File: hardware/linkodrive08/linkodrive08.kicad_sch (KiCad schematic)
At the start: 101 parts, among them J1 USB_C_Receptacle_USB2.0_16P, J2 HALL, J3 WCH_SWD, J4 LKS_SWD, J5 MOT_POWER, J6 GATE_DRIVE, J7 LOGIC_POWER, J8 MOT, Q1 WSD4070DN, Q2 WSD4070DN, Q3 WSD4070DN, Q4 WSD4070DN, Q5 WSD4070DN, Q6 WSD4070DN, U1 LKS32MC086NxQx, U3 XL1509-ADJ, U4 TPS54260, Y1 Crystal_GND24_Small

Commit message: Work on schematic; changing buck
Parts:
- added R38: 10k, symbol Device:R_Small
- added U5: LGS5145, Package_TO_SOT_SMD:SOT-23-6, symbol Regulator_Switching:LGS5145
- C2, C3: value C_Small -> 18p
- R3: value 0 -> 0R
- R32: value 124k -> 178k
- R35: value 30k -> 33k
- Y1: footprint (none) -> Crystal:Crystal_SMD_3225-4Pin_3.2x2.5mm; LCSC (none) -> C9002
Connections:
- net +3V3: now also R38.1
- net VBUS: now also Q3.2 (D)
- net WCH_~{RST}: now also R38.2
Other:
- note added: "do we need this capacitor? maybe for a motor driver"
- note removed: "do we need this?"
- moved on the sheet: C25, C26, R37

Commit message: work on design
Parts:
- removed C24: 47u, symbol Device:C_Small
- removed C25: 120n, symbol Device:C_Small
- removed C26: 82p, symbol Device:C_Small
- removed R32: 178k, symbol Device:R_Small
- removed R35: 33k, symbol Device:R_Small
- removed R36: 412k, symbol Device:R_Small
- removed R37: 15k4, symbol Device:R_Small
- removed U4: TPS54260, Package_SO:MSOP-10-1EP_3x3mm_P0.5mm_EP1.68x1.88mm, symbol Missing_Symbols:TPS54260
- C22: value 10n -> 2u2
- C23: value 47u -> 2u2
- R33: value 178k -> 120k
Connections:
- net GND: now also C23.1, U5.2 (GND); no longer C23.2
- net Vdrive: no longer C23.1
- net at JP3.1 (A): now also C22.1, U5.4 (EN), U5.5 (VIN)
- net at C21.1: now also U5.1 (BST)
- net at C21.2, D11.1 (K), L2.1: now also U5.6 (SW)
- net at R33.2, R34.1: now also U5.3 (FB)
- net at JP4.1 (A), L2.2, R33.1: now also C23.2
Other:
- note added: "Part is calculatable with kicad calculator VREF=0.812"
- note added: "VOUT calcs to 12.992V"
- note added: "稳压器电源输入。使用2.2uF或更大的陶瓷贴片尽量近旁路VIN至GND。 > Use a 2.2uF MLCC as close to VIN-GND as possible"
- moved on the sheet: C21, D11, JP3, R33, R34, U5

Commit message: Work on schematic
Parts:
- added C24, C25, C26: Cs, symbol Device:C_Small
- added J10: WCH_GPIO, symbol Connector_Generic:Conn_02x05_Odd_Even
- added J9: CAN, symbol Connector_Generic:Conn_01x02
- added NT1, NT10, NT11, NT2, NT3, NT4, NT5, NT6, NT7, NT8, NT9: NT, NetTie:NetTie-2_SMD_Pad0.5mm, symbol Device:NetTie_2
- added R32, R35, R36, R37, R39, R40: Rs, symbol Device:R_Small
- added U4: SN65HVD230, Package_SO:SOIC-8_3.9x4.9mm_P1.27mm, symbol Interface_CAN_LIN:SN65HVD230
- JP1: value NetSplit -> TX_JP
- JP2: value NetSplit -> RX_JP
- U2: value ~ -> CH32V203G6U6
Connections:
- net +3.3V is gone; now on net +3V3: J7.1 (Pin_1), U1.3 (AVDD)
- net L02 is gone; now on net LO2: U1.24 (LO2)
- net +3V3: now also J10.1 (Pin_1), U4.3 (VCC)
- net CAN_RX: now also U4.4 (R)
- net CAN_TX: now also U4.1 (D)
- net GND: now also J10.2 (Pin_2), NT5.2, U4.2 (GND), U4.8 (Rs); no longer JP2.2 (B)
- net GNDPWR: now also NT2.1, NT4.1, NT6.1, NT8.1; no longer JP1.1 (A), U1.18 (P3.7), U1.21 (P3.1), U1.39 (P3.11)
- net ISENSE_TOT+: now also NT6.2; no longer JP1.2 (B)
- net ISENSE_TOT-: now also NT5.1; no longer JP2.1 (A)
- net ISENSE_U+: now also C26.1, R39.1; no longer Q6.3 (S), R29.1
- net ISENSE_V+: now also C25.1, R36.1; no longer Q4.3 (S), R21.1
- net ISENSE_W+: now also C24.1, R32.1; no longer Q2.3 (S), R10.1
- net MOT1: now also NT11.2; no longer C15.2, U1.26 (VS1)
- net MOT2: now also NT9.2; no longer C10.2, U1.29 (VS2)
- net MOT3: now also NT10.2; no longer C6.2, U1.32 (VS3)
- net UART_FROM_WCH: now also JP1.2 (B)
- net UART_RX: now also JP1.1 (A)
- net UART_TO_WCH: now also JP2.2 (B)
- net UART_TX: now also JP2.1 (A)
- net PA4: now reaches U2.10 (PA4)
- net PA4: now also J10.5 (Pin_5)
- net PB0: now reaches U2.14 (PB0)
- net PB0: now also J10.4 (Pin_4)
- net PB1: now reaches U2.15 (PB1)
- net PB1: now also J10.6 (Pin_6)
- net PA15: now reaches U2.23 (PA15)
- net PA15: now also J10.7 (Pin_7)
- net PB3: now reaches U2.24 (PB3)
- net PB3: now also J10.8 (Pin_8)
- net PB4: now reaches U2.25 (PB4)
- net PB4: now also J10.10 (Pin_10)
- net PB5: now reaches U2.26 (PB5)
- net PB5: now also J10.9 (Pin_9)
- net PA0: now reaches U2.6 (PA0)
- net PA0: now also J10.3 (Pin_3)
- new net: NT3.1, Q2.3 (S), R10.1
- new net: NT3.2, R32.2
- new net: NT1.2, R36.2
- new net: NT8.2, R40.2
- new net: NT2.2, R37.2
- new net: NT7.1, Q6.3 (S), R29.1
- new net: NT4.2, R35.2
- new net: NT7.2, R39.2
- new net: NT1.1, Q4.3 (S), R21.1
- new net: J9.1 (Pin_1), U4.7 (CANH)
- new net: J9.2 (Pin_2), U4.6 (CANL)
- new net ISENSE_U-: C26.2, R40.1, U1.18 (P3.7)
- new net ISENSE_V-: C25.2, R37.1, U1.21 (P3.1)
- new net ISENSE_W-: C24.2, R35.1, U1.39 (P3.11)
- new net VS1: C15.2, NT11.1, U1.26 (VS1)
- new net VS2: C10.2, NT9.1, U1.29 (VS2)
- new net VS3: C6.2, NT10.1, U1.32 (VS3)
- no-connect marks 11 -> 4
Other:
- note added: "CAN"
- note added: "Jumpers are labeled from the WCH part Present incase debuging/flipping needed"
- note added: "Logic Voltage 3V3 ONLY Output only"
- note added: "Motor Out (split?)"
- note added: "Not populated due to cost"
- note added: "Place R and C near MCU"
- note added: "UART_JP"
- note removed: "Logic Voltage 3V3 ONLY"
- moved on the sheet: C13, C18, C8, J3, J7, J8, R11, R12, R18, R20, R26, R28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

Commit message: Mostly Finalise Schematic
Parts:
- removed TP1, TP2: TestPoint, symbol Connector:TestPoint
- added C27, C28, C31, C32, C35, C36: 100n, Capacitor_SMD:C_1206_3216Metric, symbol Device:C_Small
- added C29, C30, C33, C34, C37, C38: 10u, Capacitor_SMD:C_1206_3216Metric, symbol Device:C_Small
- added C39, C40: 100n, symbol Device:C_Small
- added C41, C42: 10u, symbol Device:C_Small
- added D12, D13: LED_Small, symbol Device:LED_Small
- added J11: ENC, symbol Connector_Generic:Conn_01x05
- added J12: LKS_SPI, symbol Connector_Generic:Conn_01x06
- added J13: LKS_I2C, symbol Connector_Generic:Conn_01x04
- added J14: WCH_UART_ALT, symbol Connector_Generic:Conn_01x04
- added J15: LKS_SIF, symbol Connector_Generic:Conn_01x03
- added J16: LKS_IO, symbol Connector_Generic:Conn_01x05
- added R41: 500k, symbol Device:R_Small
- added R42: 10k, symbol Device:R_Small
- added TP3: VBAT_MES, symbol Connector:TestPoint
- C1, C21: footprint (none) -> Capacitor_SMD:C_1206_3216Metric; LCSC (none) -> C24497
- C10, C15, C20, C6: footprint (none) -> Capacitor_SMD:C_0805_2012Metric
- C11, C12, C16, C17, C5, C7: value DNL -> Cg; now not fitted
- C13, C18, C8: value DNL -> Cvss
- C14, C4, C9: footprint (none) -> Capacitor_SMD:C_1206_3216Metric
- C19: value 4u7 -> 10u; footprint (none) -> Capacitor_SMD:C_1206_3216Metric; LCSC C29823 -> C13585; Voltage Tol (none) -> 15V
- L2: footprint (none) -> Capacitor_SMD:C_1206_3216Metric; LCSC (none) -> C13585
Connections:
- net +3V3: now also C27.1, C28.1, C29.1, C30.1, C31.1, C32.1, C33.1, C34.1, J11.1 (Pin_1), J12.6 (Pin_6), J13.4 (Pin_4), J14.1 (Pin_1), J15.3 (Pin_3), J16.1 (Pin_1)
- net DAC: now also J16.3 (Pin_3)
- net ENC_A: now also J11.2 (Pin_2)
- net ENC_B: now also J11.3 (Pin_3)
- net GND: now also C27.2, C28.2, C29.2, C30.2, C31.2, C32.2, C33.2, C34.2, C35.2, C36.2, C37.2, C38.2, C39.2, C40.2, C41.2, C42.2, D12.1 (K), D13.1 (K), J11.4 (Pin_4), J12.1 (Pin_1), J13.1 (Pin_1), J14.4 (Pin_4), J15.1 (Pin_1), J16.5 (Pin_5), R42.2
- net I2C_SCL: now also J13.3 (Pin_3)
- net I2C_SDA: now also J13.2 (Pin_2)
- net LED0: now also D12.2 (A)
- net LED1: now also D13.2 (A)
- net P2.2: now also J16.4 (Pin_4)
- net P2.7_LDO15: now also J16.2 (Pin_2)
- net SIF: now also J15.2 (Pin_2)
- net SPI_CLK: now also J12.5 (Pin_5)
- net SPI_CS: now also J12.2 (Pin_2)
- net SPI_DI: now also J12.4 (Pin_4)
- net SPI_DO: now also J12.3 (Pin_3)
- net VBATT_MEAS: now also R41.2, R42.1, TP3.1
- net VBUS: now also C39.1, C40.1, C41.1, C42.1, R41.1
- net Vdrive: now also C35.1, C36.1, C37.1, C38.1
- net P_ISW+: now reaches NT3.2, R32.2
- net UART_ALT_TX: now reaches U2.8 (PA2)
- net UART_ALT_TX: now also J14.2 (Pin_2)
- net P_ISV+: now reaches NT1.2, R36.2
- net P_ISU-: now reaches NT8.2, R40.2
- net P_ISV-: now reaches NT2.2, R37.2
- net P_ISW-: now reaches NT4.2, R35.2
- net P_ISU+: now reaches NT7.2, R39.2
- net UART_ALT_RX: now reaches U2.9 (PA3)
- net UART_ALT_RX: now also J14.3 (Pin_3)
- net P2.15 renamed ENC_I
- net ENC_I: now also J11.5 (Pin_5)
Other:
- note added: "DECOUPLING CAPACITORS"
- note added: "Encoder Input"
- note added: "LKS"
- note added: "LKS I2C Free for fun"
- note added: "LKS SPI Free for fun"
- note added: "MUST be placed near associated part/system"
- note added: "SIF Some one wire comms protocol Usually talks to LCDs?"
- note added: "Spare LKS IO"
- note added: "VDRIVE_REG"
- note added: "WCH"
- note added: "WCH DEBUG UART"
- moved on the sheet: C21, C22, C23, D11, JP3, JP4, L2, R33, R34, U5

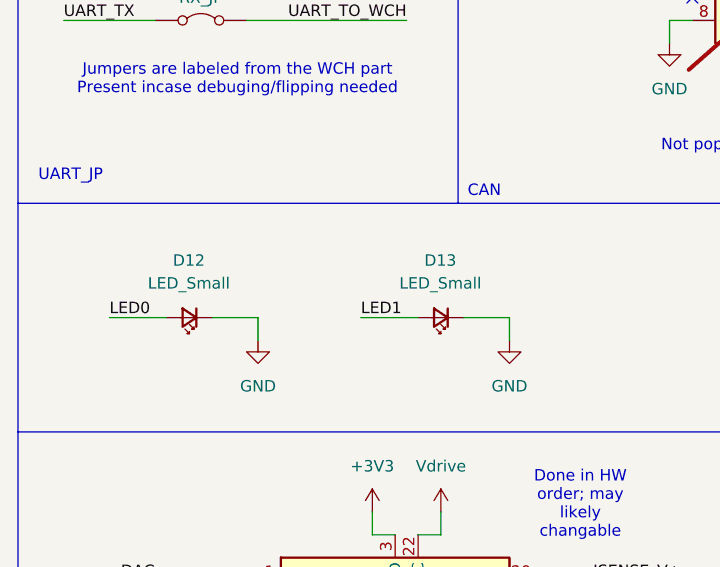
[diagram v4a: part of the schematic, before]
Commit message: Work on footprints
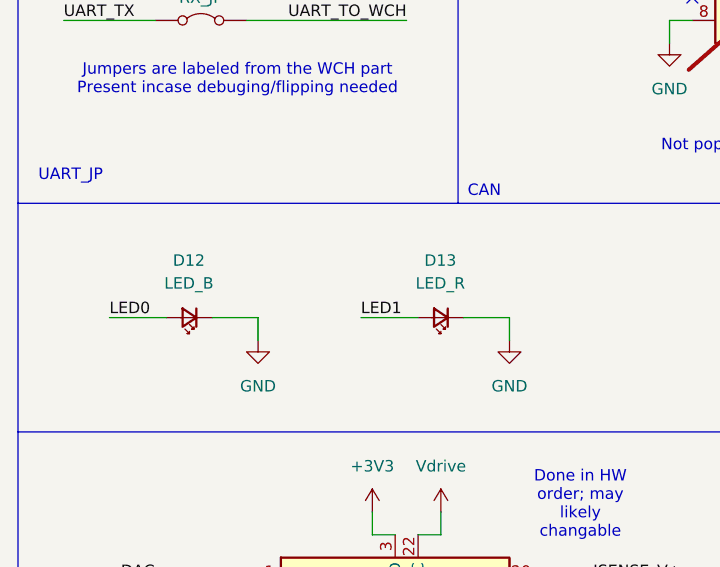
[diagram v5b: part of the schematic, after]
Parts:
- C11, C12, C13, C16, C17, C18, C24, C25, C26, C5, C7, C8: footprint (none) -> Capacitor_SMD:C_0805_2012Metric
- C2, C3: footprint (none) -> Capacitor_SMD:C_0402_1005Metric; LCSC (none) -> C1549
- C22: footprint (none) -> Capacitor_SMD:C_0805_2012Metric; LCSC (none) -> C377773; Voltage Tol (none) -> 50V
- C23: footprint (none) -> Capacitor_SMD:C_0805_2012Metric; LCSC (none) -> C377773; Voltage Tol (none) -> 15V
- C35, C36: footprint Capacitor_SMD:C_1206_3216Metric -> Capacitor_SMD:C_0603_1608Metric; LCSC C24497 -> C14663
- C39, C40, C41, C42: footprint (none) -> Capacitor_SMD:C_0603_1608Metric; LCSC (none) -> C14663
- D12: value LED_Small -> LED_B
- D13: value LED_Small -> LED_R
- JP1, JP2, JP3, JP4: footprint (none) -> Jumper:SolderJumper-2_P1.3mm_Bridged2Bar_RoundedPad1.0x1.5mm
- L1: footprint (none) -> Inductor_SMD:L_Taiyo-Yuden_NR-60xx
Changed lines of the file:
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@@
 			)
 		)
-		(property "Footprint" ""
+		(property "Footprint" "Capacitor_SMD:C_0805_2012Metric"
 			(at 185.42 257.81 0)
 			(effects
@@
 			)
 		)
-		(property "Footprint" ""
+		(property "Footprint" "Capacitor_SMD:C_0805_2012Metric"
 			(at 363.22 199.39 0)
 			(effects
@@
 			)
 		)
-		(property "Footprint" ""
+		(property "Footprint" "Capacitor_SMD:C_0805_2012Metric"
 			(at 234.95 199.39 0)
 			(effects
@@
 			)
 		)
-		(property "Footprint" ""
+		(property "Footprint" "Capacitor_SMD:C_0805_2012Metric"
 			(at 332.74 109.22 0)
 			(effects
@@
 			)
 		)
+		(property "LCSC" "C377773"
+			(at 332.74 109.22 0)
+			(effects
+				(font
+					(size 1.27 1.27)
+				)
+				(hide yes)
+			)
+		)
+		(property "Voltage Tol" "50V"
+			(at 332.74 109.22 0)
+			(effects
+				(font
+					(size 1.27 1.27)
+				)
+				(hide yes)
+			)
+		)
 		(pin "2"
 		)
@@
 			)
 		)
-		(property "Footprint" ""
+		(property "Footprint" "Capacitor_SMD:C_0805_2012Metric"
 			(at 312.42 217.17 0)
 			(effects
@@
 			)
 		)
-		(property "Footprint" ""
+		(property "Footprint" "Capacitor_SMD:C_0805_2012Metric"
 			(at 396.24 106.68 0)
 			(effects
@@
 			)
 		)
+		(property "LCSC" "C377773"
+			(at 396.24 106.68 0)
+			(effects
+				(font
+					(size 1.27 1.27)
+				)
+				(hide yes)
+			)
+		)
+		(property "Voltage Tol" "15V"
+			(at 396.24 106.68 0)
+			(effects
+				(font
+					(size 1.27 1.27)
+				)
+				(hide yes)
+			)
+		)
 		(pin "2"
 		)
@@
 			)
 		)
-		(property "Footprint" ""
+		(property "Footprint" "Capacitor_SMD:C_0805_2012Metric"
 			(at 351.79 220.98 0)
 			(effects
@@
 			)
 		)
-		(property "Footprint" ""
+		(property "Footprint" "Jumper:SolderJumper-2_P1.3mm_Bridged2Bar_RoundedPad1.0x1.5mm"
 			(at 34.29 139.7 0)
 			(effects
@@
 			)
 		)
-		(property "Footprint" ""
+		(property "Footprint" "Capacitor_SMD:C_0805_2012Metric"
 			(at 224.79 274.32 0)
 			(effects
@@
 			)
 		)
-		(property "Footprint" "Capacitor_SMD:C_1206_3216Metric"
+		(property "Footprint" "Capacitor_SMD:C_0603_1608Metric"
 			(at 254 127 0)
 			(effects
@@
 			)
 		)
-		(property "LCSC" "C24497"
+		(property "LCSC" "C14663"
 			(at 254 127 0)
 			(effects
@@
 			)
 		)
-		(property "Footprint" ""
+		(property "Footprint" "Jumper:SolderJumper-2_P1.3mm_Bridged2Bar_RoundedPad1.0x1.5mm"
 			(at 318.77 99.06 0)
 			(effects
@@
 			)
 		)
-		(property "Footprint" ""
+		(property "Footprint" "Capacitor_SMD:C_0805_2012Metric"
 			(at 184.15 204.47 0)
 			(effects
@@
 			)
 		)
-		(property "Footprint" ""
+		(property "Footprint" "Capacitor_SMD:C_0603_1608Metric"
 			(at 274.32 146.05 0)
 			(effects
@@
 			)
 		)
+		(property "LCSC" "C14663"
+			(at 274.32 146.05 0)
+			(effects
+				(font
+					(size 1.27 1.27)
+				)
+				(hide yes)
+			)
+		)
 		(pin "1"
 		)
@@
 			)
 		)
-		(property "Footprint" ""
+		(property "Footprint" "Capacitor_SMD:C_0805_2012Metric"
 			(at 223.52 220.98 0)
 			(effects
@@
 			)
 		)
-		(property "Footprint" ""
+		(property "Footprint" "Capacitor_SMD:C_0402_1005Metric"
 			(at 207.01 55.88 0)
 			(effects
@@
 			)
 		)
+		(property "LCSC" "C1549"
+			(at 207.01 55.88 0)
+			(effects
+				(font
+					(size 1.27 1.27)
+				)
+				(hide yes)
+			)
+		)
 		(pin "1"
 		)
@@
 			)
 		)
-		(property "Footprint" ""
+		(property "Footprint" "Capacitor_SMD:C_0603_1608Metric"
 			(at 243.84 146.05 0)
 			(effects
@@
 			)
 		)
+		(property "LCSC" "C14663"
+			(at 243.84 146.05 0)
+			(effects
+				(font
+					(size 1.27 1.27)
+				)
+				(hide yes)
+			)
+		)
 		(pin "1"
 		)
@@
 			)
 		)
-		(property "Footprint" ""
+		(property "Footprint" "Capacitor_SMD:C_0603_1608Metric"
 			(at 254 146.05 0)
 			(effects
@@
 			)
 		)
+		(property "LCSC" "C14663"
+			(at 254 146.05 0)
+			(effects
+				(font
+					(size 1.27 1.27)
+				)
+				(hide yes)
+			)
+		)
 		(pin "1"
 		)
@@
 			)
 		)
-		(property "Footprint" ""
+		(property "Footprint" "Inductor_SMD:L_Taiyo-Yuden_NR-60xx"
 			(at 361.95 43.18 0)
 			(effects
@@
 			)
 		)
-		(property "Value" "LED_Small"
+		(property "Value" "LED_B"
 			(at 32.9565 168.91 0)
 			(effects
@@
 			)
 		)
-		(property "Footprint" ""
+		(property "Footprint" "Jumper:SolderJumper-2_P1.3mm_Bridged2Bar_RoundedPad1.0x1.5mm"
 			(at 34.29 132.08 0)
 			(effects
@@
 			)
 		)
-		(property "Footprint" "Capacitor_SMD:C_1206_3216Metric"
+		(property "Footprint" "Capacitor_SMD:C_0603_1608Metric"
 			(at 243.84 127 0)
 			(effects
@@
 			)
 		)
-		(property "LCSC" "C24497"
+		(property "LCSC" "C14663"
 			(at 243.84 127 0)
 			(effects
@@
 			)
 		)
-		(property "Footprint" ""
+		(property "Footprint" "Capacitor_SMD:C_0402_1005Metric"
 			(at 207.01 60.96 0)
 			(effects
@@
 			)
 		)
+		(property "LCSC" "C1549"
+			(at 207.01 60.96 0)
+			(effects
+				(font
+					(size 1.27 1.27)
+				)
+				(hide yes)
+			)
+		)
 		(pin "1"
 		)
@@
 			)
 		)
-		(property "Footprint" ""
+		(property "Footprint" "Capacitor_SMD:C_0805_2012Metric"
 			(at 234.95 252.73 0)
 			(effects
@@
 			)
 		)
-		(property "Footprint" ""
+		(property "Footprint" "Capacitor_SMD:C_0603_1608Metric"
 			(at 264.16 146.05 0)
 			(effects
@@
 			)
 		)
+		(property "LCSC" "C14663"
+			(at 264.16 146.05 0)
+			(effects
+				(font
+					(size 1.27 1.27)
+				)
+				(hide yes)
+			)
+		)
 		(pin "1"
 		)
@@
 			)
 		)
-		(property "Footprint" ""
+		(property "Footprint" "Capacitor_SMD:C_0805_2012Metric"
 			(at 312.42 204.47 0)
 			(effects
@@
 			)
 		)
-		(property "Value" "LED_Small"
+		(property "Value" "LED_R"
 			(at 60.8965 168.91 0)
 			(effects
@@
 			)
 		)
-		(property "Footprint" ""
+		(property "Footprint" "Capacitor_SMD:C_0805_2012Metric"
 			(at 184.15 217.17 0)
 			(effects
@@
 			)
 		)
-		(property "Footprint" ""
+		(property "Footprint" "Capacitor_SMD:C_0805_2012Metric"
 			(at 185.42 270.51 0)
 			(effects
@@
 			)
 		)
-		(property "Footprint" ""
+		(property "Footprint" "Jumper:SolderJumper-2_P1.3mm_Bridged2Bar_RoundedPad1.0x1.5mm"
 			(at 392.43 99.06 0)
 			(effects

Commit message: Work on component selection
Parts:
- added TP1, TP2: TestPoint, symbol Connector:TestPoint
- added TP4: WCH_VTST, symbol Connector:TestPoint
- added TP5, TP6: LKS_VTST, symbol Connector:TestPoint
- C11, C12, C16, C17, C5, C7: Tolerances (none) -> 15V
- C19, C23, C35, C36, C37, C38: Tolerances (none) -> 15V; Voltage Tol 15V -> (none)
- C22, C39, C40, C41, C42: Tolerances (none) -> 50V; Voltage Tol 50V -> (none)
- D1, D10, D4, D7: footprint (none) -> Diode_SMD:D_SMA
- D2, D3, D5, D6, D8, D9: value ES2JF -> ES2DB; footprint (none) -> Diode_SMD:D_SMB; LCSC C7420342 -> C162764; Tolerances (none) -> 200V
- J1: footprint (none) -> Connector_USB:USB_C_Receptacle_G-Switch_GT-USB-7010ASV; LCSC (none) -> C2765186
- J15, J16: now not fitted
- R10, R13, R21, R29: footprint (none) -> Resistor_SMD:R_2512_6332Metric
- R12, R20, R28, R34, R38, R4, R42: footprint (none) -> Resistor_SMD:R_0603_1608Metric; LCSC (none) -> C25804
- R14, R22, R5: footprint (none) -> Resistor_SMD:R_0603_1608Metric; LCSC (none) -> C23164
- R15, R17, R23, R25, R6, R8: footprint (none) -> Resistor_SMD:R_0603_1608Metric; LCSC (none) -> C22859
- R16, R19, R24, R27, R7, R9: footprint (none) -> Resistor_SMD:R_0603_1608Metric; LCSC (none) -> C23197
- U3: LCSC (none) -> C74192
- U4: LCSC (none) -> C12084
- U5: LCSC (none) -> C5123971
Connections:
- net +3V3: now also TP4.1, TP5.1
- net UART_RX: now also TP1.1
- net UART_TX: now also TP2.1
- net Vdrive: now also TP6.1
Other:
- note added: "Voltage TSTs place near assoc. components"

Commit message: schematic rework and more parts
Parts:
- removed C30, C33, C34, C37, C38: 10u, Capacitor_SMD:C_1206_3216Metric, symbol Device:C_Small
- removed C35, C39, C40: 100n, Capacitor_SMD:C_0603_1608Metric, symbol Device:C_Small
- removed C41, C42: 10u, Capacitor_SMD:C_0603_1608Metric, symbol Device:C_Small
- added C30: 100u, Capacitor_SMD:CP_Elec_6.3x7.7, symbol Device:C_Polarized_Small
- added C33, C34, C35: 100u, MISSING, symbol Device:C_Polarized_Small
- added R43: 100k, symbol Device:R_Small
- added R44, R45: 1k, symbol Device:R_Small
- C1, C21, C27, C31, C32: footprint Capacitor_SMD:C_1206_3216Metric -> Capacitor_SMD:C_0603_1608Metric; LCSC C24497 -> C14663
- C10, C15, C6: Tolerances (none) -> 15V
- C11, C12, C16, C17, C24, C25, C26, C5, C7: footprint Capacitor_SMD:C_0805_2012Metric -> Capacitor_SMD:C_0603_1608Metric
- C13, C18, C8: value Cvss -> 1n; footprint Capacitor_SMD:C_0805_2012Metric -> Capacitor_SMD:C_0603_1608Metric; LCSC (none) -> C1588
- C14, C29, C4, C9: footprint Capacitor_SMD:C_1206_3216Metric -> Capacitor_SMD:C_0805_2012Metric; LCSC C13585 -> C440198
- C20: footprint Capacitor_SMD:C_0805_2012Metric -> Capacitor_SMD:C_0603_1608Metric; LCSC C1779 -> C19666
- C22: LCSC C377773 -> C2981733
- C28: value 100n -> 4u7; footprint Capacitor_SMD:C_1206_3216Metric -> Capacitor_SMD:C_0603_1608Metric; LCSC C24497 -> C19666
- C36: value 100n -> 100u; footprint Capacitor_SMD:C_0603_1608Metric -> Capacitor_SMD:C_1206_3216Metric; LCSC C14663 -> (none); Tolerances 15V -> (none); now not fitted
- D11: footprint (none) -> Diode_SMD:D_SOD-123; LCSC (none) -> C28646289
- D12: value LED_B -> LED_G; footprint (none) -> LED_SMD:LED_0805_2012Metric; LCSC (none) -> C2297
- D13: footprint (none) -> LED_SMD:LED_0603_1608Metric; LCSC (none) -> C2286
- D2, D3, D5, D6, D8, D9: Tolerances 200V -> (none)
- J14: now not fitted
- J3, J4: footprint (none) -> Connector:Tag-Connect_TC2030-IDC-NL_2x03_P1.27mm_Vertical
- L2: value 10u -> 10uH; footprint Capacitor_SMD:C_1206_3216Metric -> (none)
- R11, R18, R26: value 56k -> 39k
- R12, R20, R28: value 10k -> 1k; footprint Resistor_SMD:R_0603_1608Metric -> (none); LCSC C25804 -> (none)
- R3: footprint (none) -> Jumper:SolderJumper-2_P1.3mm_Bridged_Pad1.0x1.5mm
- TP1: value TestPoint -> LKS_RX; footprint (none) -> TestPoint:TestPoint_Pad_1.5x1.5mm
- TP2: value TestPoint -> LKS_TX; footprint (none) -> TestPoint:TestPoint_Pad_1.5x1.5mm
- TP3, TP4, TP6: footprint (none) -> TestPoint:TestPoint_Pad_1.5x1.5mm
- TP5: value LKS_VTST -> LKS_3V3TST; footprint (none) -> TestPoint:TestPoint_Pad_1.5x1.5mm
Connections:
- net +3V3: now also C36.1; no longer C28.1
- net GND: now also C30.2, R44.2, R45.2; no longer D12.1 (K), D13.1 (K)
- net GNDPWR: now also C33.2, C34.2, C35.2, R43.2
- net VBUS: now also C33.1, C34.1, C35.1, R43.1; no longer C14.1, C4.1, C9.1, D1.2 (A), D4.2 (A), D7.2 (A)
- net Vdrive: now also C14.1, C23.2, C28.1, C4.1, C9.1, D1.2 (A), D4.2 (A), D7.2 (A), C30.1; no longer C36.1
- net at JP4.1 (A), L2.2, R33.1: no longer C23.2
- new net: D12.1 (K), R45.1
- new net: D13.1 (K), R44.1
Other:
- note added: "General bulk cap"
- note added: "Left Intentionally Blank"
- note added: "Likely not needed LKS EVB has 220u on 3v3 Unsure why"
- note added: "Place 1 per driver phase discharge resistor wherever"
- note added: "UART Test Points"
- note removed: "VDRIVE_REG"
- moved on the sheet: C23, C29, C31, C32, TP1, TP2
